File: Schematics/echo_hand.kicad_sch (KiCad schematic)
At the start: 24 parts, among them M1 9G Servo, M10 Vibration Motor, M2 9G Servo, M3 9G Servo, M4 9G Servo, M5 9G Servo, M6 Vibration Motor, M7 Vibration Motor, M8 Vibration Motor, M9 Vibration Motor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

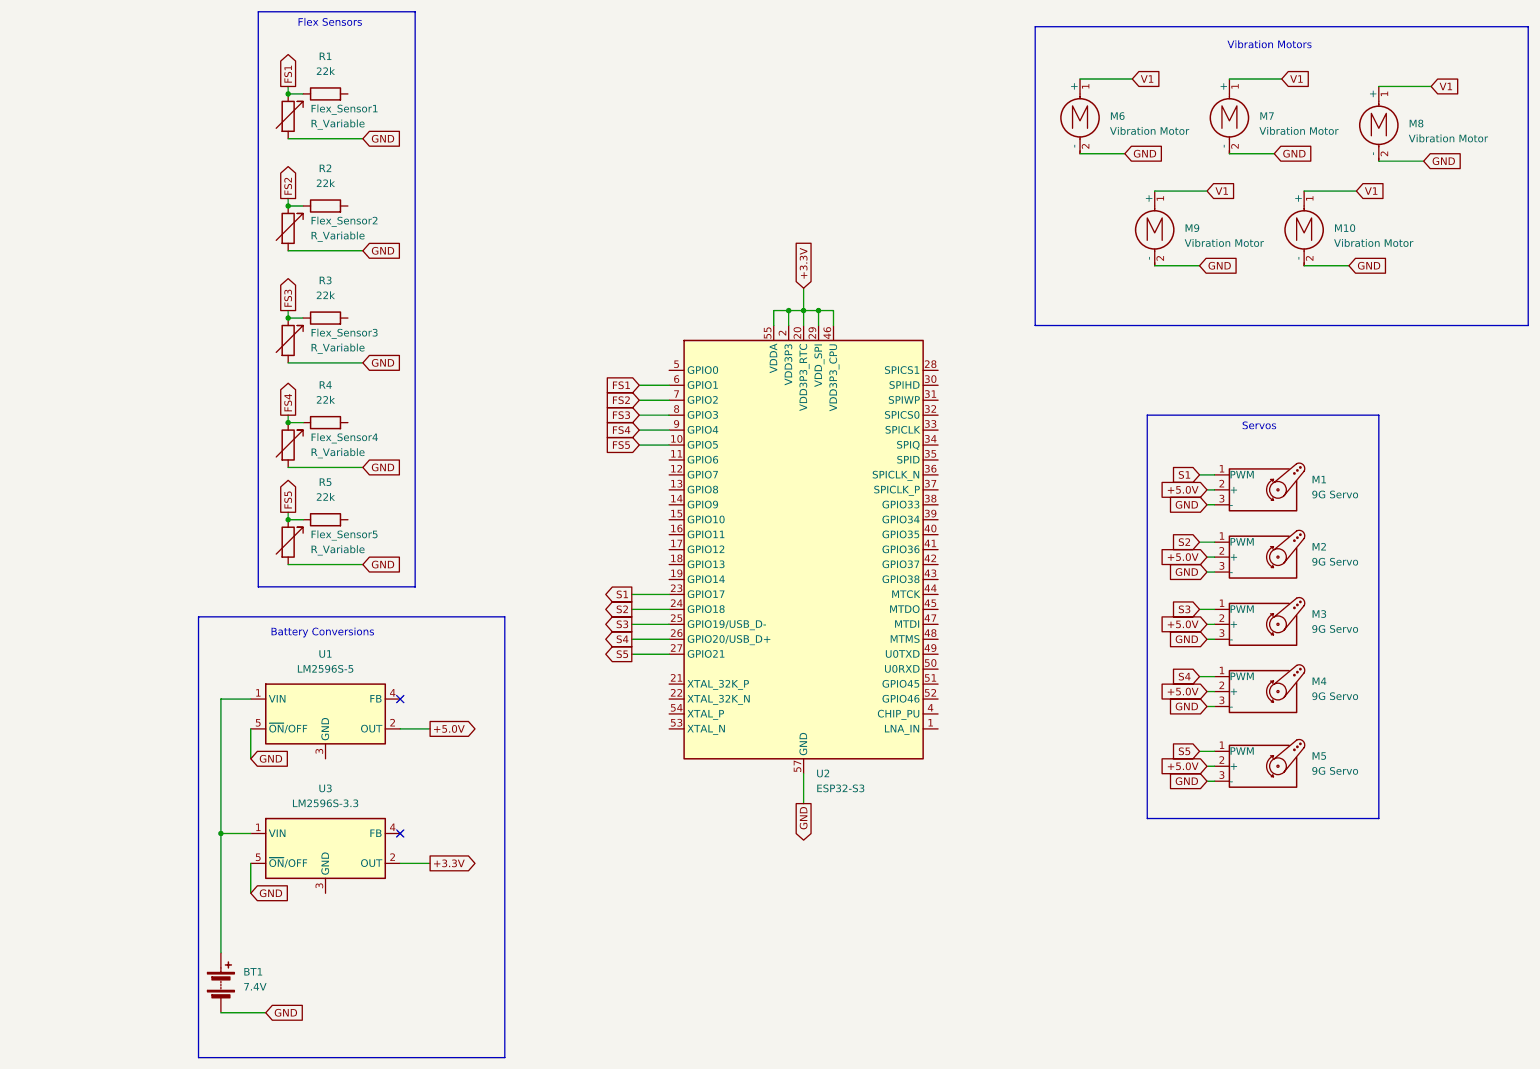
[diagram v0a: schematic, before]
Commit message: Add joystick and controller buttons
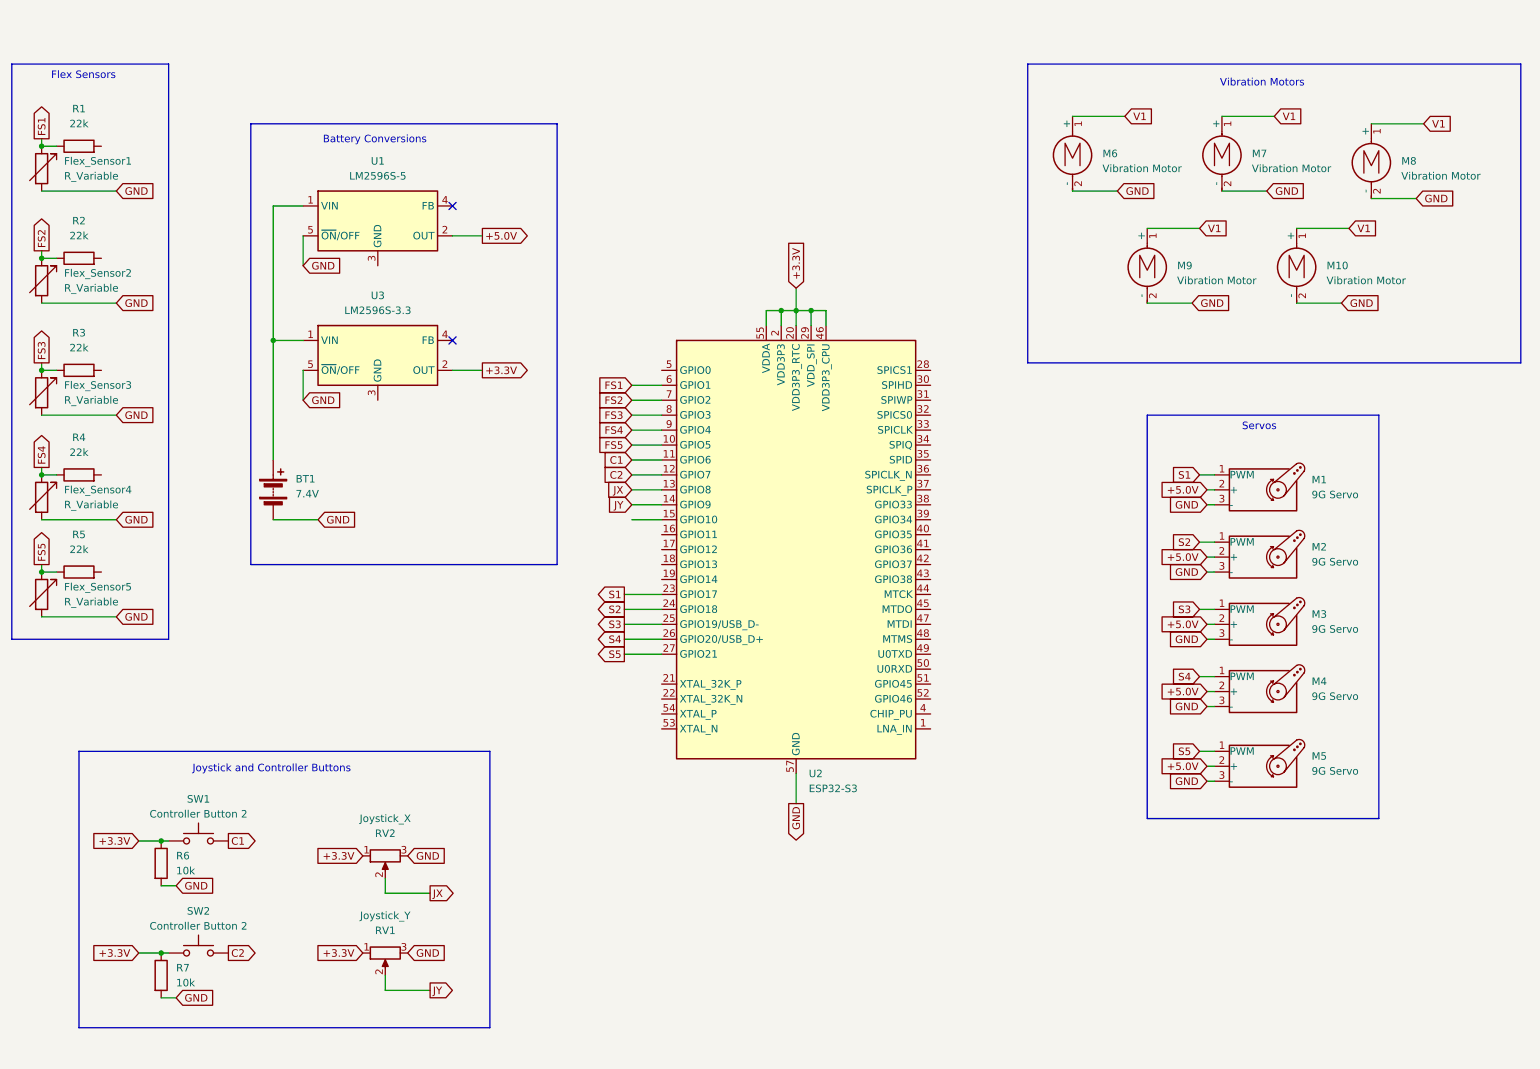
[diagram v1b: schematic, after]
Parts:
- added R6, R7: 10k, symbol Device:R
- added RV1: Joystick_Y, symbol Device:R_Potentiometer
- added RV2: Joystick_X, symbol Device:R_Potentiometer
- added SW1, SW2: Controller Button 2, symbol Switch:SW_Push
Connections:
- net +3.3V: now also R6.1, R7.1, RV1.1, RV2.1, SW1.1, SW2.1
- net GND: now also R6.2, R7.2, RV1.3, RV2.3
- net C1: now reaches U2.11 (GPIO6)
- net C1: now also SW1.2
- net C2: now reaches U2.12 (GPIO7)
- net C2: now also SW2.2
- net JX: now reaches U2.13 (GPIO8)
- net JX: now also RV2.2
- net JY: now reaches U2.14 (GPIO9)
- net JY: now also RV1.2
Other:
- note added: "Joystick and Controller Buttons"
- moved on the sheet: BT1, Flex_Sensor1, Flex_Sensor2, Flex_Sensor3, Flex_Sensor4, Flex_Sensor5, M10, M6, M7, M8, M9, R1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
